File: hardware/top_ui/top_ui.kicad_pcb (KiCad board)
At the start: 4 copper layers, 47 x 47 mm, 22 parts, among them J2 J_STK_A, J3 J_STK_B, J5 ER-TFT1.69-3, J6 Stern Klinke, Q1 BC847, Q2 P-FET 20V 1A, SW1 BTN1, SW2 BTN2, SW3 BTN3, SW4 BTN4, U2 SHT40-AD1B, U3 VL53L1X

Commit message: Display nach Datenblatt verdrahtet - und die Beleuchtung bekommt einen Treiber
Das Datenblatt ER-TFT1.69-3 liegt vor, als Auszug gesichert in
docs/datasheets/. Zwei Dinge daraus aendern den Schaltplan.

DAS RASTER IST 0,50 mm, nicht 0,7 wie bei der Loetvariante. Das provisorisch
gewaehlte Footprint TE 1-1734839-2 stimmt also.

DIE PINBELEGUNG WAR KOMPLETT FALSCH. Sie stammte vom alten Platzhalter:

  war                        ist laut Datenblatt
  1 3V3   2 GND              1 TE     2 GND
  3 SCK   4 SDA              3 RS     4 RESET
  5 DC    6 frei             5 SDA    6 SCL
  7 frei  8 CS               7 CS     8 VCC
  9 RESET 10 BL              9 IOVCC  10 LEDA
  11 GND  12 GND             11 LEDK  12 GND

Kein einziger Pin lag richtig. Haette man so bestellt, waere 3,3 V auf den
TE-Ausgang des Displays gegangen und der Takt auf den Reset.

DIE HINTERGRUNDBELEUCHTUNG BRAUCHT EINEN TREIBER. Das Datenblatt nennt 45 mA
typisch und 60 mA maximal bei Vf = 3,0 bis 3,2 V, drei LEDs parallel. Bisher
hing LEDA direkt an DISP_BL - an einem GPIO des ESP32, ueber zwei
Steckkontakte des Stapels hinweg. Das haette den Pin ueberlastet.

Aus 3,3 V geht es auch mit Vorwiderstand nicht: Bei Vf zwischen 3,0 und 3,2 V
blieben 0,1 bis 0,3 V uebrig, der Strom schwankte um den Faktor drei allein
ueber die Bauteiltoleranz. Neu deshalb aus der 5-V-Schiene:

  R_BL   39 Ohm von 5V_SYS nach LEDA   (5,0-3,1)/45mA = 42 Ohm, 86 mW
  Q_BL   N-FET an der KATHODE, Gate an DISP_BL
  R_BLG  100k Pulldown - Beleuchtung aus, solange der ESP32 nicht bootet

Ohne den Pulldown leuchtet das Display beim Einschalten unkontrolliert auf.

  top_ui  20 -> 23 Bauteile, 52 -> 55 Netze

Co-Authored-By: Claude Opus 5 (1M context) <noreply@anthropic.com>
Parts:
- added Q_BL: N-FET 30V 1A, SOT-23, B.Cu at (0.00, 2.08)
- added R_BL: 39R, R_0603_1608Metric, B.Cu at (0.78, 4.98)
- added R_BLG: 100k, R_0603_1608Metric, B.Cu at (-0.78, -0.82)
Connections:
- J5 pad 1: 3V3_SYS -> DISP_TE
- J5 pad 10: DISP_BL -> DISP_LEDA
- J5 pad 11: PGND -> DISP_LEDK
- J5 pad 3: QSPI_CLK -> QSPI_D1
- J5 pad 4: QSPI_D0 -> DISP_RST
- J5 pad 5: QSPI_D1 -> QSPI_D0
- J5 pad 6: QSPI_D2 -> QSPI_CLK
- J5 pad 7: QSPI_D3 -> DISP_CS
- J5 pad 8: DISP_CS -> 3V3_SYS
- J5 pad 9: DISP_RST -> 3V3_SYS

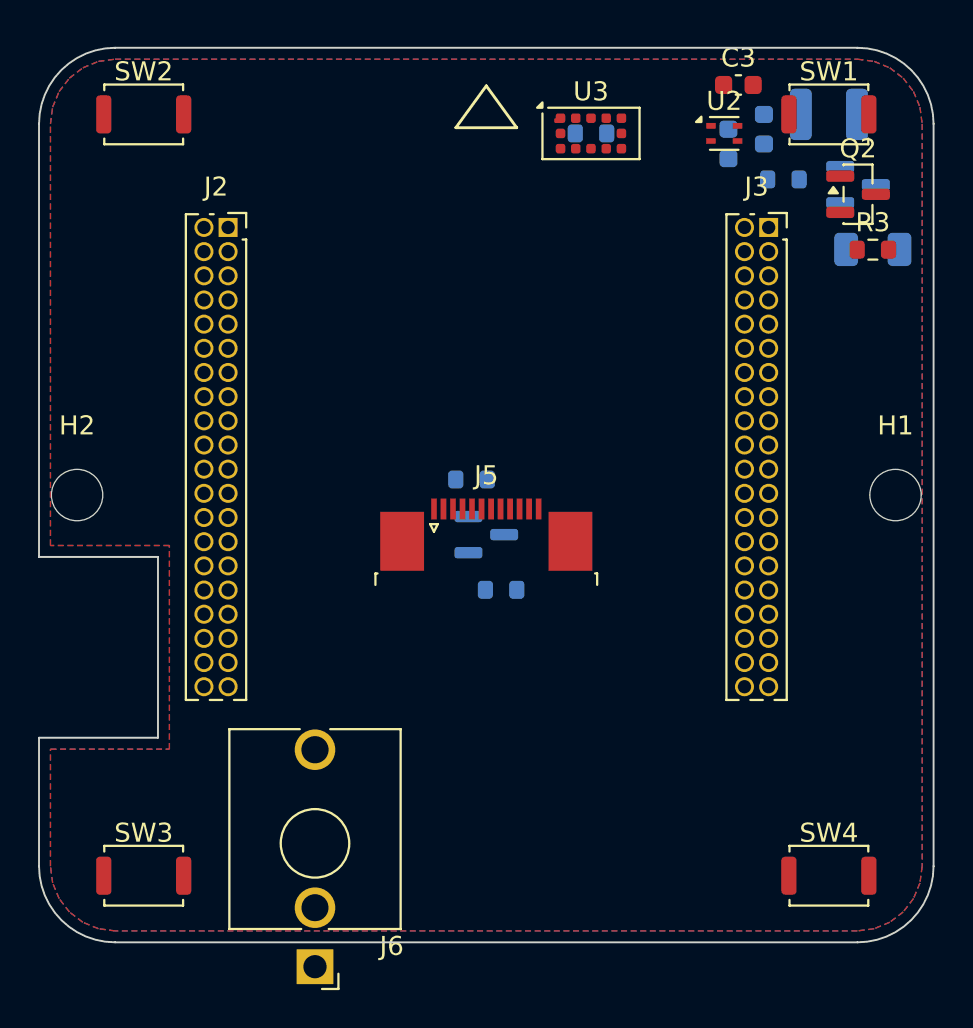
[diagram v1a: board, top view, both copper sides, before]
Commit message: Stackverbinder und FPC-Buchse auf die richtigen Seiten
DIE STACKVERBINDER SASSEN AUF ALLEN DREI BOARDS AUF DER VORDERSEITE. Drei
gleiche Buchsen auf drei Vorderseiten koennen nicht ineinandergreifen - das
war als Beschaffungsfrage bekannt (docs/06, Punkt 23), aber niemand hatte
gepruefte, was es fuer die Platzierung bedeutet.

Auf Top stand die Buchse genau dort, wo das Displaypanel aufliegen soll:
8 mm hoch, mitten unter der Klebeflaeche. Das Panel haette nirgends
aufliegen koennen.

Der Koerper gehoert jeweils auf die Seite, die zum naechsten Board zeigt:

  Bottom  F traegt den Feldstecker und zeigt in den Kabelraum -> B
  Mid     F zeigt zu Top, dort steht auch die USB-Buchse      -> F
  Top     B zeigt zu Mid, Vorderseite bleibt fuers Panel      -> B

Mid braucht damit einen echten STAPELverbinder: Buchse auf der einen Seite,
lange Stifte auf der anderen. Das ist Punkt 23, und daran haengt auch der
Plattenabstand.

J5 IST EBENFALLS AUF DIE RUECKSEITE GEWANDERT. Eine FPC-Buchse von 1,2 mm
Hoehe unter einem aufgeklebten Panel geht nicht. Die Fahne ist 18,15 mm lang
und laut Zeichnung ohnehin gefaltet - sie greift um die Boardkante.

Alle drei Boards platzieren fehlerfrei. Im Panelbereich steht vorn nur noch
die Klinkenbuchse - und die passt dort nicht mehr hin, siehe naechster
Commit.

Co-Authored-By: Claude Opus 5 (1M context) <noreply@anthropic.com>
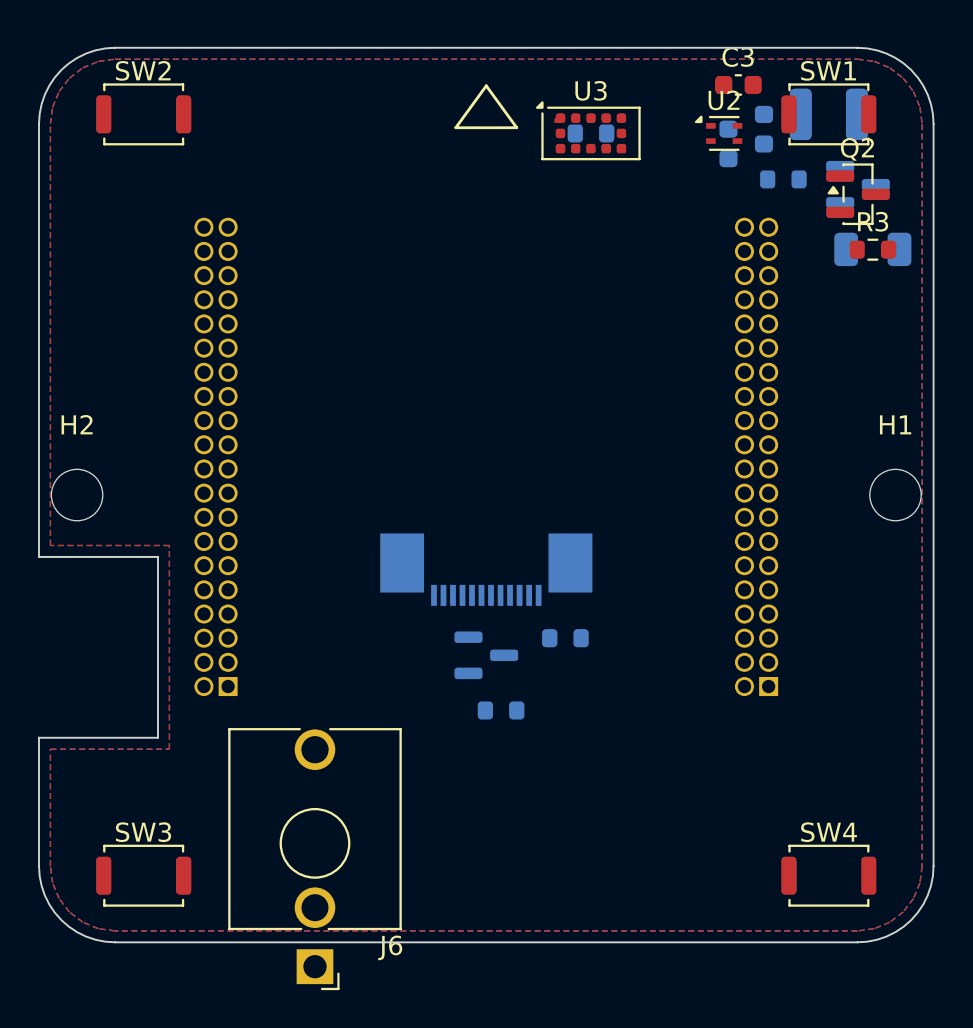
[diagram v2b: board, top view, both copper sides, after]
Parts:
- J2, J3, J5: moved to B.Cu
- moved J2 24.1 mm to (-13.6, 10.1)
- moved J3 24.1 mm to (14.8, 10.1)
- moved R_BLG 12.2 mm to (0.78, 11.3)
- moved Q_BL 6.34 mm to (0.00, 8.42)
- moved R_BL 4.23 mm to (4.16, 7.52)
- moved J5 1.84 mm to (0.00, 3.92)

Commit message: Sternanschluss: JST GH statt Klinke, und die Panelflaeche wird gesperrt
DIE KLINKE PASSTE NICHT MEHR. Mit dem Displaypanel (30,07 x 37,43, mittig
ueber dem Scheibenfenster) bleibt darunter ein Streifen von 8,16 mm. Die
3,5-mm-Klinke misst 9,0 x 12,48 und braucht selbst quergelegt 9,0 mm.

Fuer zwei Litzen bei 80 mA war sie ohnehin ueberdimensioniert. Gemessen
wurden alle zweipoligen JST-Bauformen mit 3D-Modell:

  liegend  JST SH SM02B-SRSS-TB   2,96 mm hoch   passt unter die Scheibe
  stehend  JST GH BM02B-GHS-TBT   4,20 mm hoch   braucht eine Oeffnung
  stehend  JST SH BM02B-SRSS-TB   4,32 mm hoch
  stehend  JST PH B2B-PH-K        9,40 mm hoch

Ueber der Platine sind bis zur Scheibeninnenseite 3,50 mm frei - nur die
liegende SH bliebe ganz darunter.

GEWAEHLT: JST GH stehend, unten links bei (-10 / 19,4), mit einer Oeffnung
von rund 6 x 5 mm in der Zentralscheibe. Sie hat eine Verriegelung, und man
kommt ohne Abnehmen der Scheibe an den Stecker. Der Verbinder sitzt mit
0,73 mm Abstand zum Panel und 0,77 mm zum Boardrand.

DIE PANELFLAECHE IST JETZT GESPERRT. block_f deckt den Panelumriss plus
0,5 mm Klebefuge ab - vorher wanderte der Stern-P-FET mit einer Ecke
hinein, und vor dem Seitenwechsel standen dort die Stackverbinder.

BEFESTIGUNG DES PANELS in docs/04 festgehalten: geklebt auf die
Platinenvorderseite, umlaufend auf den Rand ausserhalb der aktiven Flaeche
(2,40 mm lange Seite, 1,05 mm kurze). Die Schaumdichtung fuellt die 1,90 mm
zur Scheibe, drueckt an und haelt Staub ab - darf aber NICHT die Befestigung
sein, denn die Scheibe ist wegen USB bewusst abnehmbar.

Co-Authored-By: Claude Opus 5 (1M context) <noreply@anthropic.com>
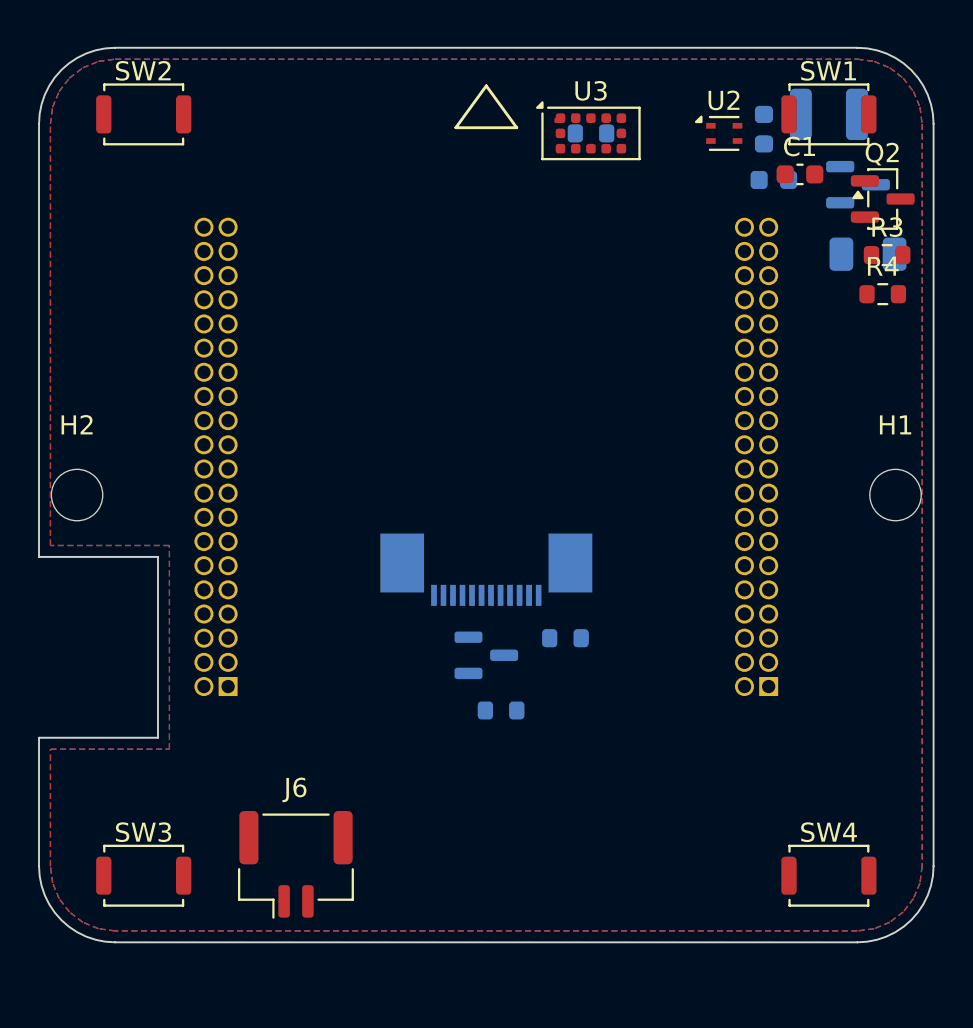
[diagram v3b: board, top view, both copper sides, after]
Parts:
- C1, R4: moved to F.Cu
- C3: moved to B.Cu
- J6: value Stern Klinke -> Stern; footprint Jack_3.5mm_QingPu_WQP-PJ398SM_Vertical_CircularHoles -> JST_GH_BM02B-GHS-TBT_1x02-1MP_P1.25mm_Vertical
- moved R4 7.98 mm to (20.8, -10.6)
- moved J6 5.47 mm to (-10.0, 19.4), turned to 0 degrees
- moved C4 3.05 mm to (15.1, -16.6), turned to 0 degrees
- moved C1 3.04 mm to (16.5, -16.8), turned to 0 degrees
- moved C3 2.68 mm to (14.6, -19.2), turned to 90 degrees
- moved Q2 1.32 mm to (20.8, -15.6)
- moved R3 0.80 mm to (21.1, -12.6)
- moved F1 0.36 mm to (20.1, -12.7)

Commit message: Alle drei Boards kupferfehlerfrei, und die Bilder zeigen endlich die Stecker
ROUTING. Alle drei Platinen haben jetzt null Kupferfehler:

  Top     179 Segmente,  22 Vias,  7 Signale offen  (vorher 11, 2 Fehler)
  Mid     720 Segmente,  74 Vias,  4 Signale offen  (vorher  6)
  Bottom  811 Segmente,  91 Vias,  6 Signale offen  (vorher  8, 6 Fehler)

Top hatte zwei copper_edge_clearance-Fehler an der USB-C-Kerbe: Eine
BTN2-Bahn lief auf In1.Cu quer durch den Ausschnitt. Der Randkeepout des
Routers kannte die Kerbe gar nicht - er bestand aus vier Balken entlang der
Kanten, und die Kerbe schneidet in eine dieser Kanten hinein. Die einzige
Aussparung darin stammte noch von der Klinkenbuchse, die es nicht mehr gibt.
route_boards.py setzt jetzt NOTCH_KEEPOUT.

M1_ISNS AUF BOTTOM IST MIT ABSICHT LEER. Freerouting hatte das analoge
Motorstrom-Messsignal auf F.Cu direkt an die Vergleichsschwelle V_TRIP_LO
gepresst - vier Kurzschluesse, eine Kreuzung, ein Abstandsfehler, alle in
einem Feld von zwei Millimetern. Einzeln herausgeloeste Segmente haben das
Problem nur verschoben: nach jedem Eingriff dieselben zwei Netze an der
naechsten Stelle. Das Netz ist deshalb komplett entfernt und wird von Hand
gezogen. Sachlich ist die Paarung ohnehin die schlechteste denkbare - koppeln
Messsignal und Ausloeseschwelle, verstimmt sich die Hinderniserkennung
selbst, ohne dass eine DRC das je bemerkt. docs/16 erklaert es samt Auflagen.

DIE BILDER ZEIGTEN DIE STECKVERBINDER NICHT - und es lag nicht an den
Modellen. Die Bildkette war nie ein Skript, sondern jedes Mal von Hand
getippt. Dadurch stammten die Teile aus verschiedenen Zeitpunkten: Modelle
16:04, Stapel-STEPs 15:59, Unterseiten-Renderings 13:41. Ausgerechnet die
Unterseiten zeigen den Feldstecker und die USB-Buchse.

tools/render_all.py macht daraus einen Aufruf: sechs Boardansichten, drei
STEP-Ausgaben mit Modellen, das Stapelbild und die Gesamtbaugruppe - ein
Zeitstand fuer alles. Renderings jetzt mit transparentem Hintergrund, damit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
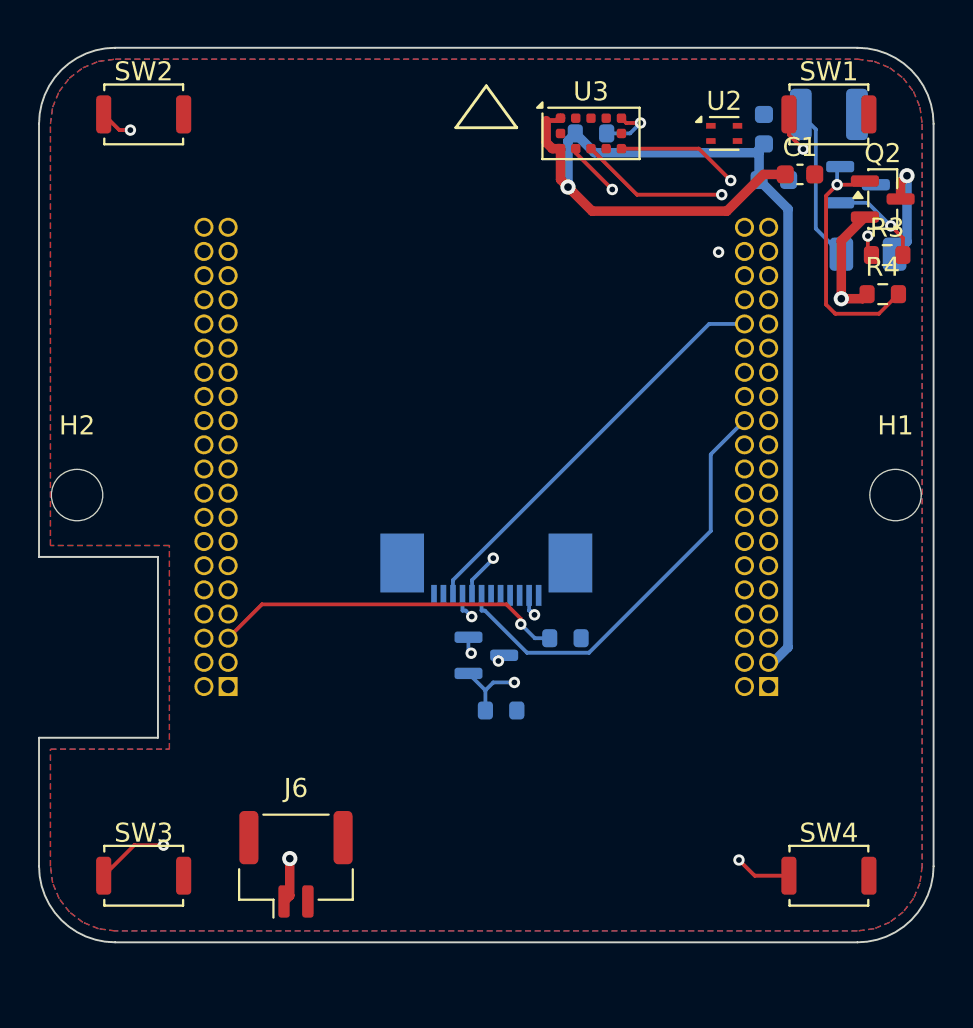
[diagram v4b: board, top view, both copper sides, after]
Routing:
- net 3V3_SYS: track 0.00 -> 90.6 mm, vias 0 -> 1
- net STAR_OUT: track 0.00 -> 70.1 mm, vias 0 -> 2
- net 6V2_STAR_F: track 0.00 -> 48.5 mm, vias 0 -> 1
- net DISP_RST: track 0.00 -> 43.6 mm, vias 0 -> 1
- net STAR_EN: track 0.00 -> 41.6 mm, vias 0 -> 1
- net BTN3: track 0.00 -> 41.0 mm, vias 0 -> 1
- net BTN4: track 0.00 -> 39.4 mm, vias 0 -> 1
- net I2C_SCL: track 0.00 -> 38.0 mm, vias 0 -> 1
- net I2C_SDA: track 0.00 -> 35.7 mm, vias 0 -> 1
- net QSPI_D0: track 0.00 -> 34.8 mm, vias 0 -> 1
- net BTN2: track 0.00 -> 32.6 mm, vias 0 -> 1
- net DISP_BL: track 0.00 -> 32.4 mm, vias 0 -> 2
- net BTN1: track 0.00 -> 31.5 mm, vias 0 -> 1
- net QSPI_CLK: track 0.00 -> 22.9 mm
- net PRESENCE_INT: track 0.00 -> 22.8 mm, vias 0 -> 1
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
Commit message: Der Stern wird magnetisch angelegt - und der Kontakt geht durch das Top-Board
ENTSCHEIDUNG: Der Stern wird nicht mehr gesteckt, sondern ueber einen
magnetischen Kontakt in der Zentralscheibe angelegt. Geschaltet wird er wie
bisher aus ESPHome ueber STAR_EN und Q2 - das haengt nicht am Steckertyp,
sondern an der Schaltung, und die bleibt unveraendert. Der Nebeneffekt der
Firmware-Schaltung ist aber wichtig: Die offen liegenden Kontakte auf der
Sichtflaeche fuehren nur dann Spannung, wenn der Stern eingeschaltet ist.

WARUM DER KONTAKT DURCH DIE PLATINE MUSS. Vor dem Top-Board sind 3,50 mm
frei (Sichtflaeche 1,0 + Druckkreuze 1,5 + Taster 2,0). Kein handelsueblicher
Magnetkontakt baut so flach; das gemessene Teil DCX-909-(9x8)-H5.2 braucht
5,20 mm. Durch einen Durchbruch taucht sein Koerper nach HINTEN in die 10 mm
zwischen Top und Mid - dort ist Platz im Ueberfluss, und die Bauhoehe ist
damit kein Kriterium mehr.

DER DURCHMESSER BLEIBT EINES. Zwischen der Sperrflaeche des Displaypanels
(y = 15,90) und der Platinenkante (23,50) liegen 7,60 mm. Mit 0,3 mm zum
Panel und 0,5 mm zur Kante passen hoechstens 6,80 mm Loch. Eingetragen sind
6,70 mm fuer einen Koerper von 6,50 mm. Das gemessene DCX-909 hat 8,00 mm
und passt NICHT - _pruefe_magnetloch() bricht mit dieser Rechnung ab, statt
ein Loch unter das aufgeklebte Panel zu schneiden. Gegen den echten Wert
getestet: wird abgewiesen.

J6 SITZT JETZT AUF DER RUECKSEITE und ist nicht mehr der Sternanschluss,
sondern die interne Verbindung zum Magnetkontakt. Vorne ging es nicht mehr
auf. Aus dem Datenblatt der GH-Serie, gegen die eigene Annahme geprueft:

  stehend BM02B 4,05 mm, gesteckt mit GHR-02V-S rund 5,7 mm
  liegend SM02B 4,25 mm, gesteckt 4,25 mm

Die LIEGENDE Bauform ist also die flachere Loesung - aber nur gesteckt; nackt
ist sie die hoehere. Beide sprengen die 3,50 mm. Hinten sind 10 mm frei, die
stehende Bauform bleibt damit unveraendert, und der enge Streifen neben dem
Display wird frei. J6 rueckt ausserdem von 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
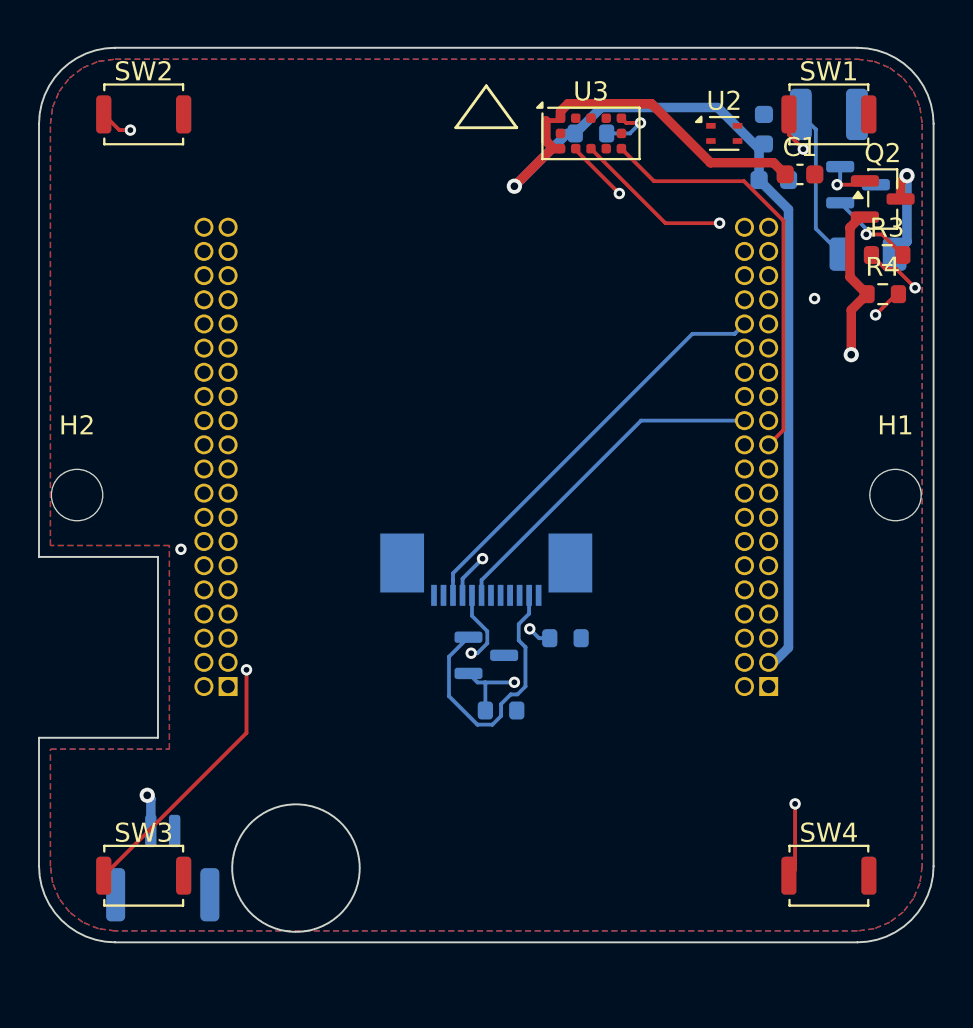
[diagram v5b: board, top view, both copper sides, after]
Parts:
- J6: value Stern -> Stern (intern); moved to B.Cu
- moved J6 7.00 mm to (-17.0, 19.6)
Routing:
- net DISP_RST: track 43.6 -> 30.6 mm
- net DISP_LEDK: track 6.31 -> 14.5 mm, vias 2 -> 0
- net QSPI_D0: track 34.8 -> 41.5 mm
- net 6V2_STAR_F: track 48.5 -> 53.9 mm
- net QSPI_CLK: track 22.9 -> 18.1 mm
- net STAR_EN: track 41.6 -> 46.0 mm
- net 3V3_SYS: track 90.6 -> 94.8 mm
- net BTN4: track 39.4 -> 35.6 mm, vias 1 -> 2
- net STAR_OUT: track 70.1 -> 67.7 mm
- net I2C_SCL: track 38.0 -> 36.0 mm
- net I2C_SDA: track 35.7 -> 34.0 mm
- net STAR_G: track 13.5 -> 11.9 mm, vias 1 -> 2
- net 5V_SYS: track 22.3 -> 21.1 mm
- net BTN3: track 41.0 -> 40.2 mm
- net DISP_BL: track 32.4 -> 31.7 mm, vias 2 -> 1
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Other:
- outline, holes or cut-outs redrawn
